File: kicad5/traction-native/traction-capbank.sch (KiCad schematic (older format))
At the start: 26 parts

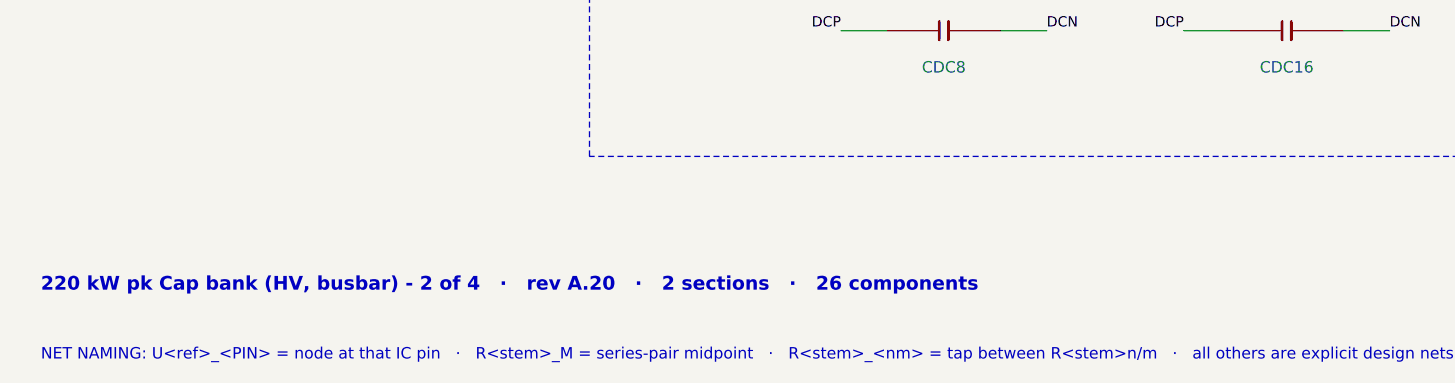
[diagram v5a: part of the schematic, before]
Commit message: Rev A.21: round 22 — three rechecks of 0ff44d9 (F209) + the layout handoff (F210–F213): every KiCad symbol bound to a footprint in a shipped traction.pretty (45 verbatim KiCad-10 patterns + 18 datasheet-drawn), fp-lib-table and per-board projects in all sets, pad-per-pin KiCad proof; NCV4276C 5-lead lands, ALM2402/TPS55340 thermal-pad pins, 2-pad crystal; QP §0.2 baseline and stale IDs; docs/layout-handoff.md
Co-Authored-By: Claude Fable 5.1 <noreply@anthropic.com>
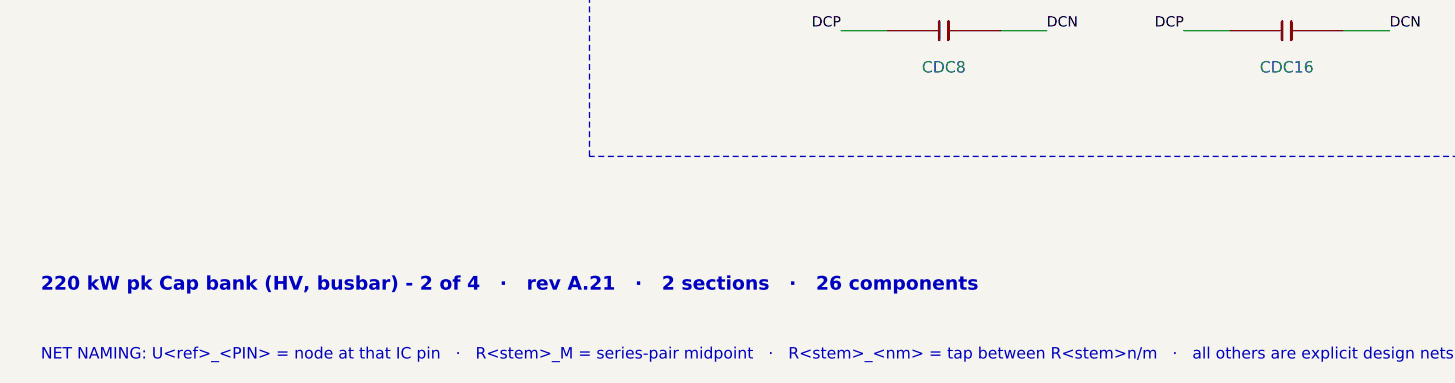
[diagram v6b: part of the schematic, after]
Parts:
- CDC1, CDC10, CDC11, CDC12, CDC13, CDC14, CDC15, CDC16, CDC2, CDC3, CDC4, CDC5, CDC6, CDC7, CDC8, CDC9: footprint FilmCan37.5 -> traction:Faratronic_C3D1_P37.5
- JCBDN, JCBDP: footprint StudM6 -> traction:MountingHole_6.4mm_M6_Pad
- JCBEN, JCBEP: footprint StudM8 -> traction:MountingHole_8.4mm_M8_Pad
- JCBUN, JCBUP, JCBVN, JCBVP, JCBWN, JCBWP: footprint TabM6 -> traction:MountingHole_6.4mm_M6_Pad
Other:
- note added: "220 kW pk Cap bank (HV, busbar) - 2 of 4 · rev A.21 · 2 sections · 26 components"
- note removed: "220 kW pk Cap bank (HV, busbar) - 2 of 4 · rev A.20 · 2 sections · 26 components"
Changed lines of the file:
@@
 Title "Traction Inverter — Cap bank (busbar assembly, 320 uF)"
 Date "2026-09-23"
-Rev "A.20"
+Rev "A.21"
 Comp "Traction Inverter 220 kW pk - Cap bank (HV, busbar), sheet 2 of 4"
 Comment1 "Inverter = Power board + Cap bank busbar + bolt-on Discharge board (all HV) + Control card (LV); safe state holds with any link lost"
@@
 $EndDescr
 Text Notes 600 5100 0    60   ~ 12
-220 kW pk Cap bank (HV, busbar) - 2 of 4   ·   rev A.20   ·   2 sections   ·   26 components
+220 kW pk Cap bank (HV, busbar) - 2 of 4   ·   rev A.21   ·   2 sections   ·   26 components
 Text Notes 600 5400 0    50   ~ 0
 NET NAMING: U<ref>_<PIN> = node at that IC pin   ·   R<stem>_M = series-pair midpoint   ·   R<stem>_<nm> = tap between R<stem>n/m   ·   all others are explicit design nets   ·   same name on another sheet = same net, joined only at the named connector/stud/tab
@@
 F 0 "JCBDN" H 1250 2190 50  0000 C CNN
 F 1 "STUD-M6" H 1250 2520 50  0000 C CNN
-F 2 "StudM6" H 1250 2350 50  0001 C CNN
+F 2 "traction:MountingHole_6.4mm_M6_Pad" H 1250 2350 50  0001 C CNN
 F 3 "~" H 1250 2350 50  0001 C CNN
 F 4 "CLASS" H 1250 2350 50  0001 C CNN "LCSC"
@@
 F 0 "JCBDP" H 1250 1790 50  0000 C CNN
 F 1 "STUD-M6" H 1250 2120 50  0000 C CNN
-F 2 "StudM6" H 1250 1950 50  0001 C CNN
+F 2 "traction:MountingHole_6.4mm_M6_Pad" H 1250 1950 50  0001 C CNN
 F 3 "~" H 1250 1950 50  0001 C CNN
 F 4 "CLASS" H 1250 1950 50  0001 C CNN "LCSC"
@@
 F 0 "JCBEN" H 1250 1390 50  0000 C CNN
 F 1 "STUD-M8" H 1250 1720 50  0000 C CNN
-F 2 "StudM8" H 1250 1550 50  0001 C CNN
+F 2 "traction:MountingHole_8.4mm_M8_Pad" H 1250 1550 50  0001 C CNN
 F 3 "~" H 1250 1550 50  0001 C CNN
 F 4 "CLASS" H 1250 1550 50  0001 C CNN "LCSC"
@@
 F 0 "JCBEP" H 1250 990 50  0000 C CNN
 F 1 "STUD-M8" H 1250 1320 50  0000 C CNN
-F 2 "StudM8" H 1250 1150 50  0001 C CNN
+F 2 "traction:MountingHole_8.4mm_M8_Pad" H 1250 1150 50  0001 C CNN
 F 3 "~" H 1250 1150 50  0001 C CNN
 F 4 "CLASS" H 1250 1150 50  0001 C CNN "LCSC"
@@
 F 0 "JCBUN" H 2150 1390 50  0000 C CNN
 F 1 "TAB-M6" H 2150 1720 50  0000 C CNN
-F 2 "TabM6" H 2150 1550 50  0001 C CNN
+F 2 "traction:MountingHole_6.4mm_M6_Pad" H 2150 1550 50  0001 C CNN
 F 3 "~" H 2150 1550 50  0001 C CNN
 F 4 "CLASS" H 2150 1550 50  0001 C CNN "LCSC"
@@
 F 0 "JCBUP" H 2150 990 50  0000 C CNN
 F 1 "TAB-M6" H 2150 1320 50  0000 C CNN
-F 2 "TabM6" H 2150 1150 50  0001 C CNN
+F 2 "traction:MountingHole_6.4mm_M6_Pad" H 2150 1150 50  0001 C CNN
 F 3 "~" H 2150 1150 50  0001 C CNN
 F 4 "CLASS" H 2150 1150 50  0001 C CNN "LCSC"
@@
 F 0 "JCBVN" H 2150 2190 50  0000 C CNN
 F 1 "TAB-M6" H 2150 2520 50  0000 C CNN
-F 2 "TabM6" H 2150 2350 50  0001 C CNN
+F 2 "traction:MountingHole_6.4mm_M6_Pad" H 2150 2350 50  0001 C CNN
 F 3 "~" H 2150 2350 50  0001 C CNN
 F 4 "CLASS" H 2150 2350 50  0001 C CNN "LCSC"
@@
 F 0 "JCBVP" H 2150 1790 50  0000 C CNN
 F 1 "TAB-M6" H 2150 2120 50  0000 C CNN
-F 2 "TabM6" H 2150 1950 50  0001 C CNN
+F 2 "traction:MountingHole_6.4mm_M6_Pad" H 2150 1950 50  0001 C CNN
 F 3 "~" H 2150 1950 50  0001 C CNN
 F 4 "CLASS" H 2150 1950 50  0001 C CNN "LCSC"
@@
 F 0 "JCBWN" H 2150 2990 50  0000 C CNN
 F 1 "TAB-M6" H 2150 3320 50  0000 C CNN
-F 2 "TabM6" H 2150 3150 50  0001 C CNN
+F 2 "traction:MountingHole_6.4mm_M6_Pad" H 2150 3150 50  0001 C CNN
 F 3 "~" H 2150 3150 50  0001 C CNN
 F 4 "CLASS" H 2150 3150 50  0001 C CNN "LCSC"
@@
 F 0 "JCBWP" H 2150 2590 50  0000 C CNN
 F 1 "TAB-M6" H 2150 2920 50  0000 C CNN
-F 2 "TabM6" H 2150 2750 50  0001 C CNN
+F 2 "traction:MountingHole_6.4mm_M6_Pad" H 2150 2750 50  0001 C CNN
 F 3 "~" H 2150 2750 50  0001 C CNN
 F 4 "CLASS" H 2150 2750 50  0001 C CNN "LCSC"
@@
 F 0 "CDC1" H 4550 990 50  0000 C CNN
 F 1 "20uF" H 4550 1320 50  0000 C CNN
-F 2 "FilmCan37.5" H 4550 1150 50  0001 C CNN
+F 2 "traction:Faratronic_C3D1_P37.5" H 4550 1150 50  0001 C CNN
 F 3 "~" H 4550 1150 50  0001 C CNN
 F 4 "C2840809" H 4550 1150 50  0001 C CNN "LCSC"
@@
 F 0 "CDC10" H 6050 1390 50  0000 C CNN
 F 1 "20uF" H 6050 1720 50  0000 C CNN
-F 2 "FilmCan37.5" H 6050 1550 50  0001 C CNN
+F 2 "traction:Faratronic_C3D1_P37.5" H 6050 1550 50  0001 C CNN
 F 3 "~" H 6050 1550 50  0001 C CNN
 F 4 "C2840809" H 6050 1550 50  0001 C CNN "LCSC"
@@
 F 0 "CDC11" H 6050 1790 50  0000 C CNN
 F 1 "20uF" H 6050 2120 50  0000 C CNN
-F 2 "FilmCan37.5" H 6050 1950 50  0001 C CNN
+F 2 "traction:Faratronic_C3D1_P37.5" H 6050 1950 50  0001 C CNN
 F 3 "~" H 6050 1950 50  0001 C CNN
 F 4 "C2840809" H 6050 1950 50  0001 C CNN "LCSC"
@@
 F 0 "CDC12" H 6050 2190 50  0000 C CNN
 F 1 "20uF" H 6050 2520 50  0000 C CNN
-F 2 "FilmCan37.5" H 6050 2350 50  0001 C CNN
+F 2 "traction:Faratronic_C3D1_P37.5" H 6050 2350 50  0001 C CNN
 F 3 "~" H 6050 2350 50  0001 C CNN
 F 4 "C2840809" H 6050 2350 50  0001 C CNN "LCSC"
@@
 F 0 "CDC13" H 6050 2590 50  0000 C CNN
 F 1 "20uF" H 6050 2920 50  0000 C CNN
-F 2 "FilmCan37.5" H 6050 2750 50  0001 C CNN
+F 2 "traction:Faratronic_C3D1_P37.5" H 6050 2750 50  0001 C CNN
 F 3 "~" H 6050 2750 50  0001 C CNN
 F 4 "C2840809" H 6050 2750 50  0001 C CNN "LCSC"
@@
 F 0 "CDC14" H 6050 2990 50  0000 C CNN
 F 1 "20uF" H 6050 3320 50  0000 C CNN
-F 2 "FilmCan37.5" H 6050 3150 50  0001 C CNN
+F 2 "traction:Faratronic_C3D1_P37.5" H 6050 3150 50  0001 C CNN
 F 3 "~" H 6050 3150 50  0001 C CNN
 F 4 "C2840809" H 6050 3150 50  0001 C CNN "LCSC"
@@
 F 0 "CDC15" H 6050 3390 50  0000 C CNN
 F 1 "20uF" H 6050 3720 50  0000 C CNN
-F 2 "FilmCan37.5" H 6050 3550 50  0001 C CNN
+F 2 "traction:Faratronic_C3D1_P37.5" H 6050 3550 50  0001 C CNN
 F 3 "~" H 6050 3550 50  0001 C CNN
 F 4 "C2840809" H 6050 3550 50  0001 C CNN "LCSC"
@@
 F 0 "CDC16" H 6050 3790 50  0000 C CNN
 F 1 "20uF" H 6050 4120 50  0000 C CNN
-F 2 "FilmCan37.5" H 6050 3950 50  0001 C CNN
+F 2 "traction:Faratronic_C3D1_P37.5" H 6050 3950 50  0001 C CNN
 F 3 "~" H 6050 3950 50  0001 C CNN
 F 4 "C2840809" H 6050 3950 50  0001 C CNN "LCSC"
@@
 F 0 "CDC2" H 4550 1390 50  0000 C CNN
 F 1 "20uF" H 4550 1720 50  0000 C CNN
-F 2 "FilmCan37.5" H 4550 1550 50  0001 C CNN
+F 2 "traction:Faratronic_C3D1_P37.5" H 4550 1550 50  0001 C CNN
 F 3 "~" H 4550 1550 50  0001 C CNN
 F 4 "C2840809" H 4550 1550 50  0001 C CNN "LCSC"
@@
 F 0 "CDC3" H 4550 1790 50  0000 C CNN
 F 1 "20uF" H 4550 2120 50  0000 C CNN
-F 2 "FilmCan37.5" H 4550 1950 50  0001 C CNN
+F 2 "traction:Faratronic_C3D1_P37.5" H 4550 1950 50  0001 C CNN
 F 3 "~" H 4550 1950 50  0001 C CNN
 F 4 "C2840809" H 4550 1950 50  0001 C CNN "LCSC"
@@
 F 0 "CDC4" H 4550 2190 50  0000 C CNN
 F 1 "20uF" H 4550 2520 50  0000 C CNN
-F 2 "FilmCan37.5" H 4550 2350 50  0001 C CNN
+F 2 "traction:Faratronic_C3D1_P37.5" H 4550 2350 50  0001 C CNN
 F 3 "~" H 4550 2350 50  0001 C CNN
 F 4 "C2840809" H 4550 2350 50  0001 C CNN "LCSC"
@@
 F 0 "CDC5" H 4550 2590 50  0000 C CNN
 F 1 "20uF" H 4550 2920 50  0000 C CNN
-F 2 "FilmCan37.5" H 4550 2750 50  0001 C CNN
+F 2 "traction:Faratronic_C3D1_P37.5" H 4550 2750 50  0001 C CNN
 F 3 "~" H 4550 2750 50  0001 C CNN
 F 4 "C2840809" H 4550 2750 50  0001 C CNN "LCSC"
@@
 F 0 "CDC6" H 4550 2990 50  0000 C CNN
 F 1 "20uF" H 4550 3320 50  0000 C CNN
-F 2 "FilmCan37.5" H 4550 3150 50  0001 C CNN
+F 2 "traction:Faratronic_C3D1_P37.5" H 4550 3150 50  0001 C CNN
 F 3 "~" H 4550 3150 50  0001 C CNN
 F 4 "C2840809" H 4550 3150 50  0001 C CNN "LCSC"
@@
 F 0 "CDC7" H 4550 3390 50  0000 C CNN
 F 1 "20uF" H 4550 3720 50  0000 C CNN
-F 2 "FilmCan37.5" H 4550 3550 50  0001 C CNN
+F 2 "traction:Faratronic_C3D1_P37.5" H 4550 3550 50  0001 C CNN
 F 3 "~" H 4550 3550 50  0001 C CNN
 F 4 "C2840809" H 4550 3550 50  0001 C CNN "LCSC"
@@
 F 0 "CDC8" H 4550 3790 50  0000 C CNN
 F 1 "20uF" H 4550 4120 50  0000 C CNN
-F 2 "FilmCan37.5" H 4550 3950 50  0001 C CNN
+F 2 "traction:Faratronic_C3D1_P37.5" H 4550 3950 50  0001 C CNN
 F 3 "~" H 4550 3950 50  0001 C CNN
 F 4 "C2840809" H 4550 3950 50  0001 C CNN "LCSC"
@@
 F 0 "CDC9" H 6050 990 50  0000 C CNN
 F 1 "20uF" H 6050 1320 50  0000 C CNN
-F 2 "FilmCan37.5" H 6050 1150 50  0001 C CNN
+F 2 "traction:Faratronic_C3D1_P37.5" H 6050 1150 50  0001 C CNN
 F 3 "~" H 6050 1150 50  0001 C CNN
 F 4 "C2840809" H 6050 1150 50  0001 C CNN "LCSC"

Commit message: Rev A.22: round 23 — rechecks of 452de85 (F214–F220), the VESC program (FW-38…FW-46, Traction Tool in Qt) and the "why not done" extension (F221–F239)
Hardware: the R2R reference isolated at ball A9 (RR2R 10 Ω + 1 µF + 100 nF, S32K39 DS note 8), the SWD header on its
surface-mount Samtec land with a mounting-technology lock in the library generator, the footprint library declared
KiCad 10.0.6+ and no longer mirrored into the KiCad 5 sets; the BOM intro follows the SKU; a VREFH window row and VR-34/35.

Firmware (TI_FW_ID 0x0A0F0015, CAL layout 4, 190 fields / 91 CAL rows, 80 DTCs): FW-37 joint torque solve with a
postcondition; the VESC gap closure — FW-38 signed field update (Ed25519, anti-rollback, ISO-TP), FW-39 interlocked motor
self-commissioning, FW-40 UDS diagnostics (0x19/0x22/0x2A/0x14 over ISO 15765-2), FW-41 fault-triggered waveform capture,
FW-42 overspeed, FW-43 run-time statistics, FW-44 key-on offset adoption, FW-45 saturation-dependent inductance tables
with gain scheduling, FW-46 cogging feed-forward; twelve defects found by the closed-loop simulator bridge (F221–F232),
the 64-bit divide out of every ISR path with a link-time guard, the UDS escape single frame accepted by every service,
the root of trust reported (DID 0xFD23), the boot record, motor data and active maps as DIDs; 421 tests / 4937 checks /
0 failed on the host (-O1, -O2, ASan/UBSan, -ffp-contract=off) and on the Cortex-M7 under QEMU with the target compiler
(make qemu-test, T-59); make target-check 63 markers, make target-size with the divide guard.

Traction Tool (tool/): Qt 6 / C++17 Widgets + Qwt, offline; pages Dashboard, Live plots, Controls, Commissioning,
Parameters, Faults & alerts, Analysis, Terminal, Firmware; transports simulator bridge (tool/bridge, the real firmware
against a plant), log replay, CAN (QCanBus with ISO-TP both ways, proved against the firmware over the virtualcan bus);
the signed update end to end over both transports; the commissioning routines, the map sw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
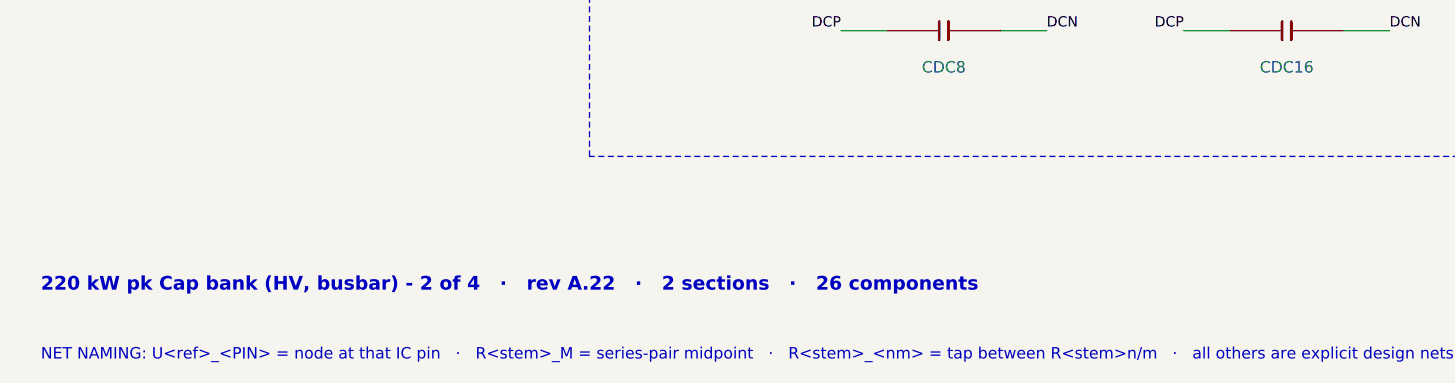
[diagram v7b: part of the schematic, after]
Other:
- note added: "220 kW pk Cap bank (HV, busbar) - 2 of 4 · rev A.22 · 2 sections · 26 components"
- note removed: "220 kW pk Cap bank (HV, busbar) - 2 of 4 · rev A.21 · 2 sections · 26 components"
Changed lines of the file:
@@
 Title "Traction Inverter — Cap bank (busbar assembly, 320 uF)"
 Date "2026-09-23"
-Rev "A.21"
+Rev "A.22"
 Comp "Traction Inverter 220 kW pk - Cap bank (HV, busbar), sheet 2 of 4"
 Comment1 "Inverter = Power board + Cap bank busbar + bolt-on Discharge board (all HV) + Control card (LV); safe state holds with any link lost"
@@
 $EndDescr
 Text Notes 600 5100 0    60   ~ 12
-220 kW pk Cap bank (HV, busbar) - 2 of 4   ·   rev A.21   ·   2 sections   ·   26 components
+220 kW pk Cap bank (HV, busbar) - 2 of 4   ·   rev A.22   ·   2 sections   ·   26 components
 Text Notes 600 5400 0    50   ~ 0
 NET NAMING: U<ref>_<PIN> = node at that IC pin   ·   R<stem>_M = series-pair midpoint   ·   R<stem>_<nm> = tap between R<stem>n/m   ·   all others are explicit design nets   ·   same name on another sheet = same net, joined only at the named connector/stud/tab

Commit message: Rev A.23: round 24 — four rechecks of 4ed0101 (F240–F244): the SDADC reference on its supply node, acquisition freshness, the map's flux slope and the ripple limiter's exact bounds, the temperature latch, the V_DC expiry
Hardware (F240, no new part): the S32K39 data sheet's SDADC table (Rev. 3 Table 38, in our archive and our own
extracted-parameters file) requires VREFP within ±25 mV of AVDD; the round-23 disposition had judged the general +100 mV
note and called the figure absent while the references sat on the FS26 VREF, matched to the SDADC-supply LDO only within
±1 %. Every non-R2R reference group (E6/H6 SAR, E10/F13 SDADC) is now on V5A itself with VDDA_SDADC and VDD_HV_A (NXP's
GEN3 arrangement); the ratiometric loads (HW_ID and offset dividers, the seven NTC pull-ups) moved with the reference; the
R2R ladder keeps the FS26 VREF as its isolated supply through the 10 Ω branch (CR2R1 330 nF, 37 kHz); CSB5 2.2 µF holds
the FS26 window alone (1.36–2.92 µF effective); the absolute SAR scale re-budgeted at the LDO2's ±1.75 %; ERC locks, pin
freeze, manifest, handoff §4.11 island rule (≤ 20 mΩ from E12 to any VREFH ball), VR-34 closed by design, IR-26, QP-TH-06.
Pipeline at A.23: ERC 981/0/0, verify 158/18/0, sim 23/6/0, Marine 87/23/0, 21 pages / 2065 pins, KiCad proof PASS, PDFs
and BOMs regenerated (₹72,983 unchanged). The handoff §6 gives every open pre-layout decision a provisional default.

Firmware (TI_FW_ID 0x0A0F0016, CAL layout 4, 191 fields / 92 CAL rows, 82 DTCs): F241 a stopped slow ADC channel stayed
valid forever (the caller discarded the acquisition stamp) → a three-state contract new/held/expired for every slow-list
input with cal_temp_hold_ms and DTC_ADC_SLOW_STALE, every slow consumer audited (V5GD/VOFS, IGN, INTRLOK_N, VSUP, HW_ID);
F242 the inductance map must keep a positive flux slope (≥ 0.25 × L0 below every breakpoint) and the ripple limiter bounds
every piece of its interval in closed form (breakpoints alone shown insufficient by a 20 000-m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
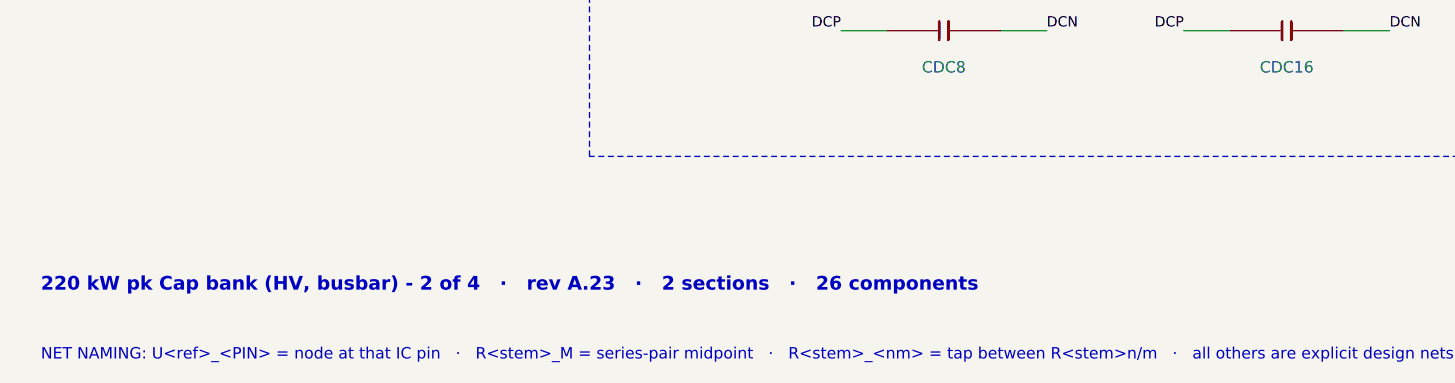
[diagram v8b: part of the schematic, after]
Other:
- note added: "220 kW pk Cap bank (HV, busbar) - 2 of 4 · rev A.23 · 2 sections · 26 components"
- note removed: "220 kW pk Cap bank (HV, busbar) - 2 of 4 · rev A.22 · 2 sections · 26 components"
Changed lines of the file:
@@
 Title "Traction Inverter — Cap bank (busbar assembly, 320 uF)"
 Date "2026-09-23"
-Rev "A.22"
+Rev "A.23"
 Comp "Traction Inverter 220 kW pk - Cap bank (HV, busbar), sheet 2 of 4"
 Comment1 "Inverter = Power board + Cap bank busbar + bolt-on Discharge board (all HV) + Control card (LV); safe state holds with any link lost"
@@
 $EndDescr
 Text Notes 600 5100 0    60   ~ 12
-220 kW pk Cap bank (HV, busbar) - 2 of 4   ·   rev A.22   ·   2 sections   ·   26 components
+220 kW pk Cap bank (HV, busbar) - 2 of 4   ·   rev A.23   ·   2 sections   ·   26 components
 Text Notes 600 5400 0    50   ~ 0
 NET NAMING: U<ref>_<PIN> = node at that IC pin   ·   R<stem>_M = series-pair midpoint   ·   R<stem>_<nm> = tap between R<stem>n/m   ·   all others are explicit design nets   ·   same name on another sheet = same net, joined only at the named connector/stud/tab
